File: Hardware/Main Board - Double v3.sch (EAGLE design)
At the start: 89 parts, among them J1 MICROMOD-2222-C, J10 MICRO-SD-PUSH-PUSH-EXT-PIN, J2 Vertical Qwiic Connector, J4 QWIIC_RIGHT_ANGLE, J5 CORTEX_JTAG_DEBUG_MINIMUM_PTH, J6 MICROMOD_FUNCTION_MAIN, J7 MICROMOD_FUNCTION_MAIN, Q1 3.1A/30V/105mΩ, Q2 20V/4.2A/52mΩ/1.4W, U1 STG3856QTR, U2 MCP73831, U3 ESD Diode, U4 AP7347DQ-33W5-7K-3.3V, U5 AP7361C-33

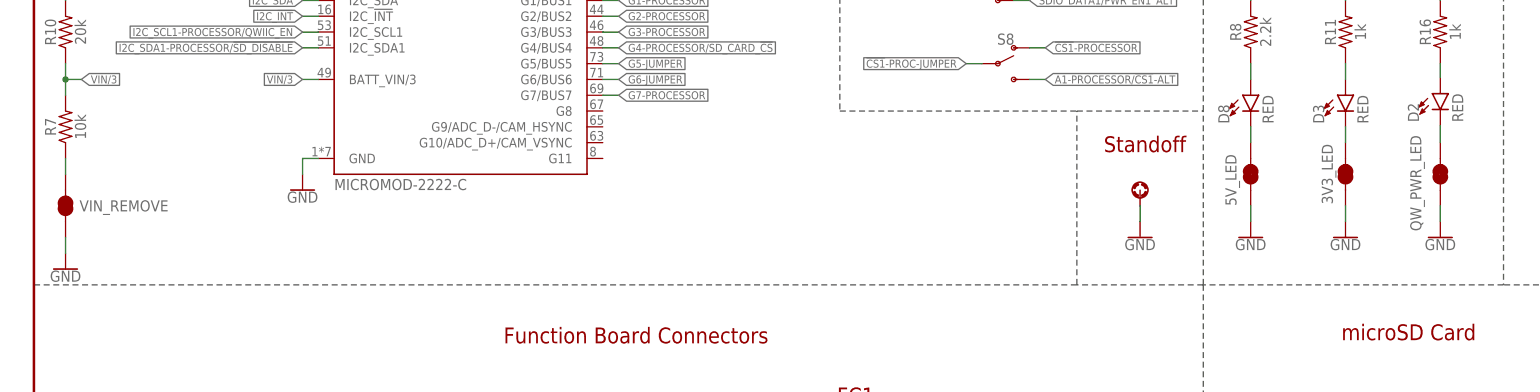
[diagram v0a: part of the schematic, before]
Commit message: Changes resistor divider jumper name and qwiic_led jumper name
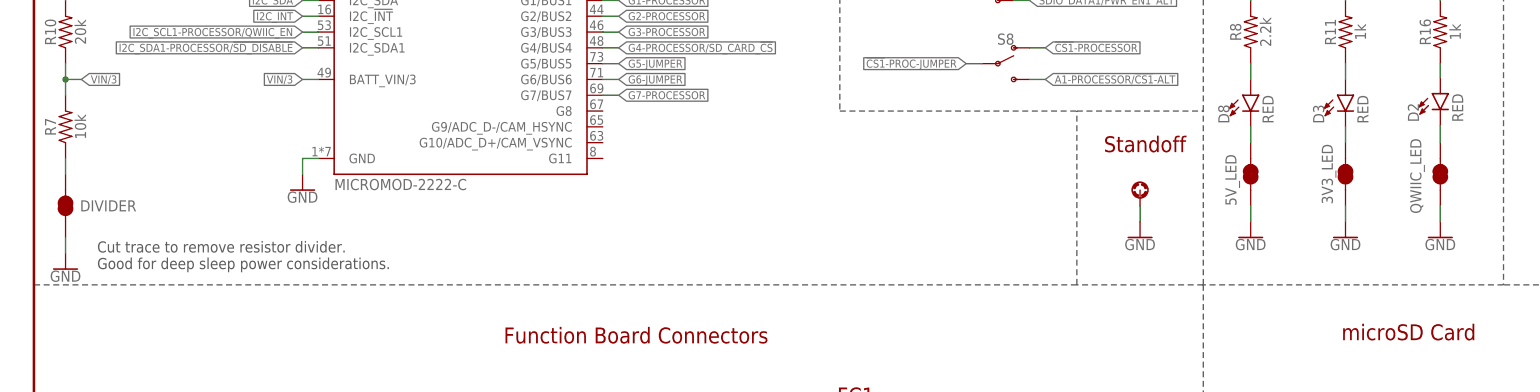
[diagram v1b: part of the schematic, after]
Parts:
- renumbered QW_PWR_LED to QWIIC_LED, VIN_REMOVE to DIVIDER
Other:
- note added: "Cut trace to remove resistor divider. Good for deep sleep power considerations."
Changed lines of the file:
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@@
 <part name="SUPPLY11" library="dip_switch" deviceset="3.3V_QWIIC" device=""/>
 <part name="SUPPLY29" library="SparkFun-PowerSymbols" deviceset="3.3V" device=""/>
-<part name="VIN_REMOVE" library="SparkFun-Jumpers" deviceset="JUMPER-SMT_2_NC_TRACE" device="_SILK" package3d_urn="urn:adsk.eagle:package:39281/1"/>
+<part name="DIVIDER" library="SparkFun-Jumpers" deviceset="JUMPER-SMT_2_NC_TRACE" device="_SILK" package3d_urn="urn:adsk.eagle:package:39281/1"/>
 <part name="D2" library="SparkFun-LED" deviceset="LED-RED" device="0603" value="RED"/>
 <part name="R16" library="SparkFun-Resistors" deviceset="1KOHM" device="-0603-1/10W-1%" value="1k"/>
-<part name="QW_PWR_LED" library="SparkFun-Jumpers" deviceset="JUMPER-SMT_2_NC_TRACE" device="_SILK" package3d_urn="urn:adsk.eagle:package:39281/1" value="JUMPER-SMT_2_NC_TRACE_SILK"/>
+<part name="QWIIC_LED" library="SparkFun-Jumpers" deviceset="JUMPER-SMT_2_NC_TRACE" device="_SILK" package3d_urn="urn:adsk.eagle:package:39281/1" value="JUMPER-SMT_2_NC_TRACE_SILK"/>
 <part name="GND30" library="SparkFun-PowerSymbols" deviceset="GND" device=""/>
 <part name="SUPPLY34" library="dip_switch" deviceset="3.3V_QWIIC" device=""/>
@@
 USB Shield from Ground. </text>
 <wire x1="274.32" y1="195.58" x2="274.32" y2="132.08" width="0.2032" layer="97" style="longdash"/>
+<text x="10.16" y="134.62" size="1.778" layer="97" font="vector">Cut trace to remove resistor divider.
+Good for deep sleep power considerations.</text>
 </plain>
 <instances>
@@
 <attribute name="VALUE" x="419.1" y="99.314" size="1.778" layer="96" font="vector" align="bottom-center"/>
 </instance>
-<instance part="VIN_REMOVE" gate="G$1" x="5.08" y="144.78" smashed="yes" rot="MR90">
-<attribute name="NAME" x="14.478" y="144.78" size="1.778" layer="95" font="vector" rot="MR0" align="center"/>
+<instance part="DIVIDER" gate="G$1" x="5.08" y="144.78" smashed="yes" rot="MR90">
+<attribute name="NAME" x="11.938" y="144.78" size="1.778" layer="95" font="vector" rot="MR0" align="center"/>
 </instance>
 <instance part="D2" gate="G$1" x="226.06" y="162.814" smashed="yes">
@@
 <attribute name="VALUE" x="227.584" y="172.72" size="1.778" layer="96" font="vector" rot="R90" align="top-center"/>
 </instance>
-<instance part="QW_PWR_LED" gate="G$1" x="226.06" y="149.86" smashed="yes" rot="R90">
-<attribute name="NAME" x="223.012" y="140.716" size="1.778" layer="95" font="vector" rot="R90"/>
+<instance part="QWIIC_LED" gate="G$1" x="226.06" y="149.86" smashed="yes" rot="R90">
+<attribute name="NAME" x="223.012" y="143.51" size="1.778" layer="95" font="vector" rot="R90"/>
 </instance>
 <instance part="GND30" gate="1" x="226.06" y="139.7" smashed="yes">
@@
 <segment>
 <pinref part="GND23" gate="1" pin="GND"/>
-<pinref part="VIN_REMOVE" gate="G$1" pin="1"/>
+<pinref part="DIVIDER" gate="G$1" pin="1"/>
 <wire x1="5.08" y1="139.7" x2="5.08" y2="137.16" width="0.1524" layer="91"/>
 </segment>
@@
 <pinref part="GND30" gate="1" pin="GND"/>
 <wire x1="226.06" y1="142.24" x2="226.06" y2="144.78" width="0.1524" layer="91"/>
-<pinref part="QW_PWR_LED" gate="G$1" pin="1"/>
+<pinref part="QWIIC_LED" gate="G$1" pin="1"/>
 </segment>
 <segment>
@@
 <net name="N$7" class="0">
 <segment>
-<pinref part="VIN_REMOVE" gate="G$1" pin="2"/>
+<pinref part="DIVIDER" gate="G$1" pin="2"/>
 <wire x1="5.08" y1="152.4" x2="5.08" y2="149.86" width="0.1524" layer="91"/>
 <pinref part="R7" gate="G$1" pin="1"/>
@@
 <net name="N$8" class="0">
 <segment>
-<pinref part="QW_PWR_LED" gate="G$1" pin="2"/>
+<pinref part="QWIIC_LED" gate="G$1" pin="2"/>
 <wire x1="226.06" y1="154.94" x2="226.06" y2="157.734" width="0.1524" layer="91"/>
 <pinref part="D2" gate="G$1" pin="C"/>

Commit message: Removes old designs, updates polygons
* Updates silk
* Uses VIN as power supply to battery charger
* Fixes PCH Mosfet
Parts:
- removed R17: 2.0M, SparkFun-Resistors:2MOHMS-0603-1/10W-1%
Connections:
- net I2C_SDA1-PROCESSOR/!SD_DISABLE! renamed I2C_SDA1-PROCESSOR/!SD_ENABLE!
- net !BOOT!: now also J6.DFU_!BOOT!, J7.DFU_!BOOT!; no longer J6.MCU_!BOOT!, J7.MCU_!BOOT!
- net !DFU-FC0!: now also J6.DFU_!ACTIVE!; no longer J6.MCU_!DFU_STAT!
- net !DFU-FC1!: now also J7.DFU_!ACTIVE!; no longer J7.MCU_!DFU_STAT!
- net !RESET!: now also J6.DFU_!RST!, J7.DFU_!RST!; no longer J6.MCU_!RST!, J7.MCU_!RST!
- net 3.3V: no longer R19.2
- net 3V3_MEAS: no longer R17.2
- net GND: now also R19.2; no longer R17.1
- net RX1-DFU_TX-FC0-PLEX: now also J6.DFU_FC_TX; no longer J6.MCU_DFU_TX
- net RX1-DFU_TX-FC1-PLEX: now also J7.DFU_FC_TX; no longer J7.MCU_DFU_TX
- net TX1-DFU_RX-FC0-PLEX: now also J6.DFU_FC_RX; no longer J6.MCU_DFU_RX
- net TX1-DFU_RX-FC1-PLEX: now also J7.DFU_FC_RX; no longer J7.MCU_DFU_RX
- net VCC: no longer C3.1, R5.1, U2.VIN
- net VIN: now also C3.1, R5.1, U2.VIN
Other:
- moved on the sheet: 3V3_MEAS, DIVIDER, J1, R10, R7
